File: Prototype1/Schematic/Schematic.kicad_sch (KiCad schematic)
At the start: 2 parts, among them P1 PMOD-Device-x2-Type-Generic-A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, U1 Teensy4.0

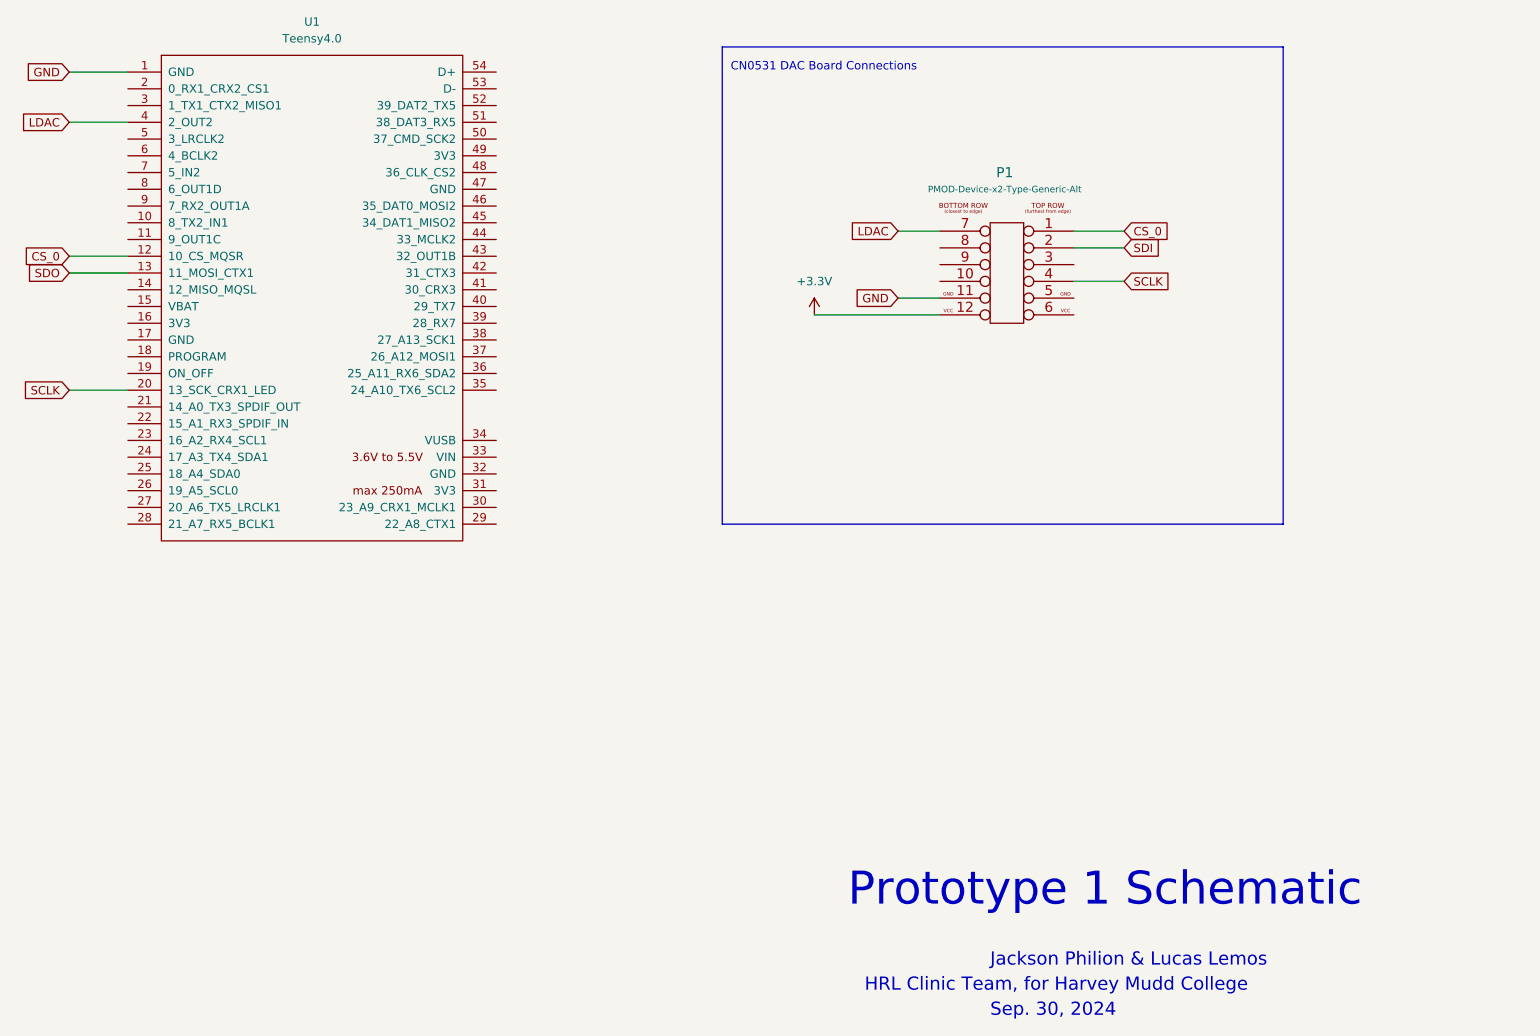
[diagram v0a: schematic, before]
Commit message: Add CD74 to Schematic
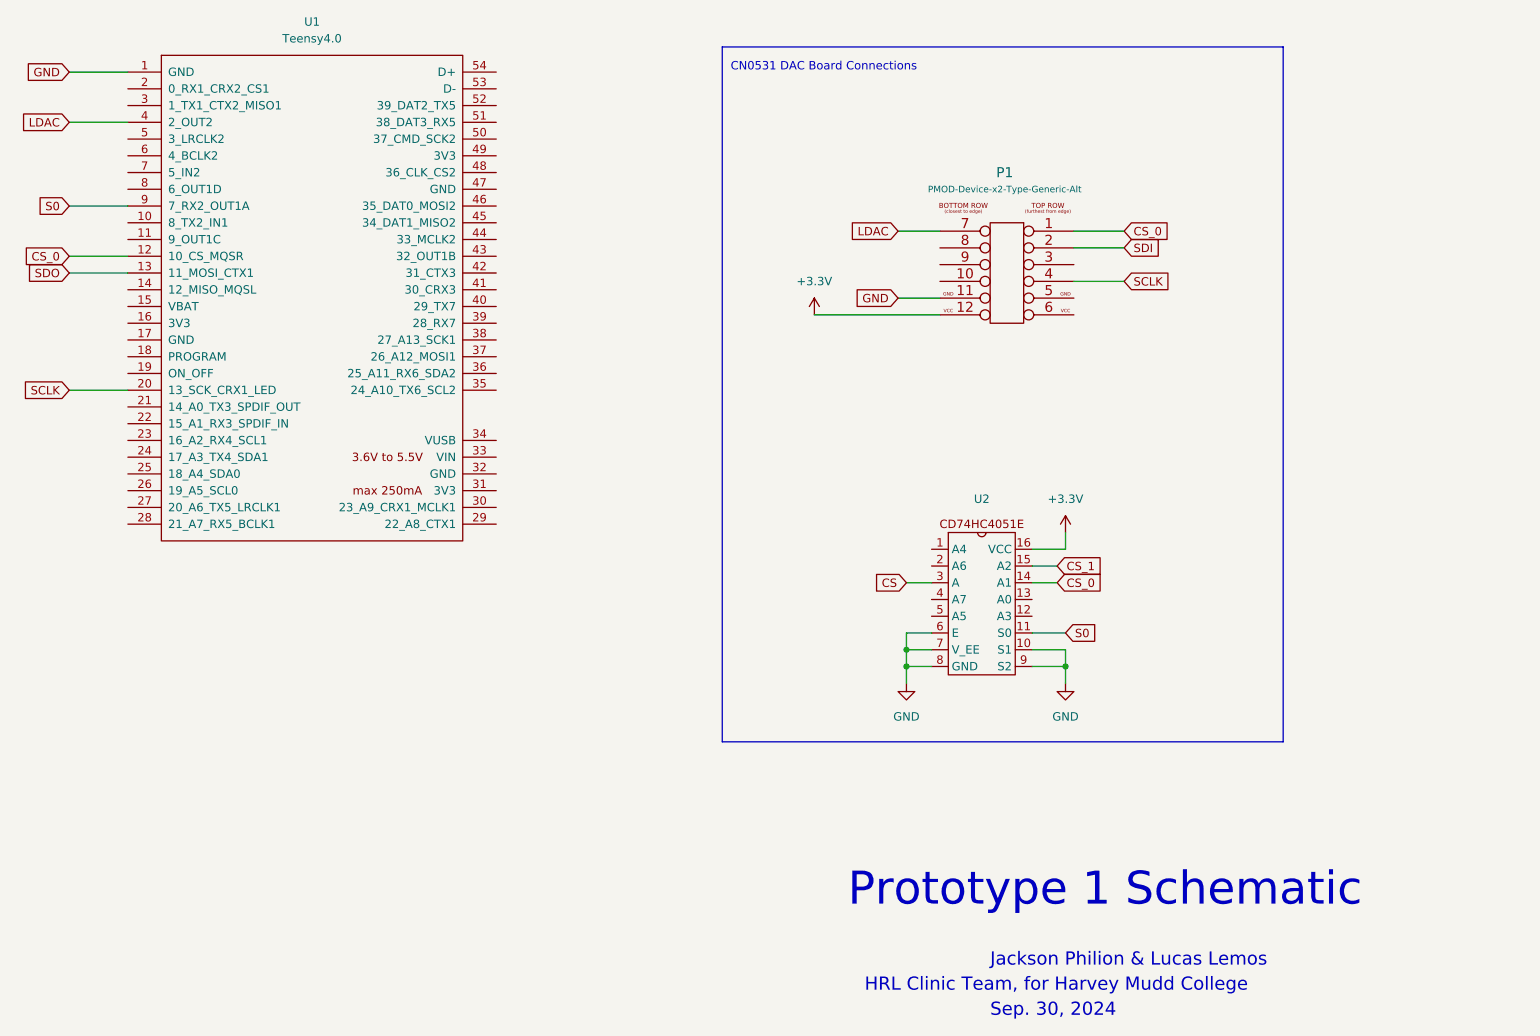
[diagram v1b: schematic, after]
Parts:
- added U2: ~, symbol HRL_Custom:CD74HC4051E
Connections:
- net +3.3V: now also U2.16 (VCC)
- net CS_0: now also U2.14 (A1)
- net GND: now also U2.10 (S1), U2.6 (E), U2.7 (V_EE), U2.8 (GND), U2.9 (S2)
- net S0: now reaches U1.9 (7_RX2_OUT1A)
- net S0: now also U2.11 (S0)
- new net CS: U2.3 (A)
- new net CS_1: U2.15 (A2)
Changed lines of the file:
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@@
 (kicad_sch (version 20230121) (generator eeschema)
   (paper "A4")
+  (junction (at 198.12 138.43) (diameter 0) (color 0 0 0 0)
+  )
+  (junction (at 198.12 140.97) (diameter 0) (color 0 0 0 0)
+  )
+  (junction (at 222.25 140.97) (diameter 0) (color 0 0 0 0)
+  )
+  (wire (pts (xy 198.12 138.43) (xy 198.12 140.97))
+    (stroke (width 0) (type default))
+  )
   (wire (pts (xy 71.12 58.42) (xy 80.01 58.42))
     (stroke (width 0) (type default))
   )
+  (wire (pts (xy 198.12 128.27) (xy 201.93 128.27))
+    (stroke (width 0) (type default))
+  )
+  (wire (pts (xy 222.25 140.97) (xy 222.25 143.51))
+    (stroke (width 0) (type default))
+  )
   (wire (pts (xy 223.52 74.93) (xy 231.14 74.93))
     (stroke (width 0) (type default))
@@
     (stroke (width 0) (type default))
   )
+  (wire (pts (xy 201.93 140.97) (xy 198.12 140.97))
+    (stroke (width 0) (type default))
+  )
   (wire (pts (xy 71.12 50.8) (xy 80.01 50.8))
     (stroke (width 0) (type default))
   )
+  (wire (pts (xy 222.25 138.43) (xy 222.25 140.97))
+    (stroke (width 0) (type default))
+  )
+  (wire (pts (xy 217.17 128.27) (xy 220.98 128.27))
+    (stroke (width 0) (type default))
+  )
   (wire (pts (xy 196.85 74.93) (xy 203.2 74.93))
     (stroke (width 0) (type default))
   )
+  (wire (pts (xy 201.93 138.43) (xy 198.12 138.43))
+    (stroke (width 0) (type default))
+  )
+  (wire (pts (xy 71.12 71.12) (xy 80.01 71.12))
+    (stroke (width 0) (type default))
+  )
+  (wire (pts (xy 217.17 135.89) (xy 222.25 135.89))
+    (stroke (width 0) (type default))
+  )
+  (wire (pts (xy 217.17 140.97) (xy 222.25 140.97))
+    (stroke (width 0) (type default))
+  )
   (wire (pts (xy 71.12 78.74) (xy 80.01 78.74))
     (stroke (width 0) (type default))
   )
+  (wire (pts (xy 198.12 135.89) (xy 198.12 138.43))
+    (stroke (width 0) (type default))
+  )
   (wire (pts (xy 71.12 81.28) (xy 80.01 81.28))
     (stroke (width 0) (type default))
   )
+  (wire (pts (xy 201.93 135.89) (xy 198.12 135.89))
+    (stroke (width 0) (type default))
+  )
+  (wire (pts (xy 217.17 138.43) (xy 222.25 138.43))
+    (stroke (width 0) (type default))
+  )
   (wire (pts (xy 223.52 77.47) (xy 231.14 77.47))
     (stroke (width 0) (type default))
@@
     (stroke (width 0) (type default))
   )
+  (wire (pts (xy 222.25 123.19) (xy 222.25 120.65))
+    (stroke (width 0) (type default))
+  )
   (wire (pts (xy 184.15 87.63) (xy 203.2 87.63))
     (stroke (width 0) (type default))
   )
-  (rectangle (start 170.18 46.99) (end 255.27 119.38)
+  (wire (pts (xy 217.17 123.19) (xy 222.25 123.19))
+    (stroke (width 0) (type default))
+  )
+  (wire (pts (xy 217.17 125.73) (xy 220.98 125.73))
+    (stroke (width 0) (type default))
+  )
+  (wire (pts (xy 198.12 140.97) (xy 198.12 143.51))
+    (stroke (width 0) (type default))
+  )
+  (rectangle (start 170.18 46.99) (end 255.27 152.4)
     (stroke (width 0) (type default))
     (fill (type none))
@@
     )
   )
+  (global_label "S0" (shape input) (at 71.12 71.12 180) (fields_autoplaced)
+    (effects (font (size 1.27 1.27)) (justify right))
+    (property "Intersheetrefs" "${INTERSHEET_REFS}" (at 65.7158 71.12 0)
+      (effects (font (size 1.27 1.27)) (justify right) hide)
+    )
+  )
   (global_label "SCLK" (shape input) (at 231.14 82.55 0) (fields_autoplaced)
     (effects (font (size 1.27 1.27)) (justify left))
@@
     )
   )
+  (global_label "CS_0" (shape input) (at 220.98 128.27 0) (fields_autoplaced)
+    (effects (font (size 1.27 1.27)) (justify left))
+    (property "Intersheetrefs" "${INTERSHEET_REFS}" (at 228.6218 128.27 0)
+      (effects (font (size 1.27 1.27)) (justify left) hide)
+    )
+  )
   (global_label "GND" (shape input) (at 71.12 50.8 180) (fields_autoplaced)
     (effects (font (size 1.27 1.27)) (justify right))
@@
     )
   )
+  (global_label "S0" (shape input) (at 222.25 135.89 0) (fields_autoplaced)
+    (effects (font (size 1.27 1.27)) (justify left))
+    (property "Intersheetrefs" "${INTERSHEET_REFS}" (at 227.6542 135.89 0)
+      (effects (font (size 1.27 1.27)) (justify left) hide)
+    )
+  )
+  (global_label "CS_1" (shape input) (at 220.98 125.73 0) (fields_autoplaced)
+    (effects (font (size 1.27 1.27)) (justify left))
+    (property "Intersheetrefs" "${INTERSHEET_REFS}" (at 228.6218 125.73 0)
+      (effects (font (size 1.27 1.27)) (justify left) hide)
+    )
+  )
   (global_label "LDAC" (shape input) (at 71.12 58.42 180) (fields_autoplaced)
     (effects (font (size 1.27 1.27)) (justify right))
@@
     (effects (font (size 1.27 1.27)) (justify right))
     (property "Intersheetrefs" "${INTERSHEET_REFS}" (at 64.3248 81.28 0)
+      (effects (font (size 1.27 1.27)) (justify right) hide)
+    )
+  )
+  (global_label "CS" (shape input) (at 198.12 128.27 180) (fields_autoplaced)
+    (effects (font (size 1.27 1.27)) (justify right))
+    (property "Intersheetrefs" "${INTERSHEET_REFS}" (at 192.6553 128.27 0)
       (effects (font (size 1.27 1.27)) (justify right) hide)
     )
@@
         (path "/4eb04ca2-2eee-448f-b097-610a5fc44453"
           (reference "P1") (unit 1)
+        )
+      )
+    )
+  )
+  (symbol (lib_id "power:GND") (at 222.25 143.51 0) (unit 1)
+    (in_bom yes) (on_board yes) (dnp no) (fields_autoplaced)
+    (property "Reference" "#PWR04" (at 222.25 149.86 0)
+      (effects (font (size 1.27 1.27)) hide)
+    )
+    (property "Value" "GND" (at 222.25 148.59 0)
+      (effects (font (size 1.27 1.27)))
+    )
+    (property "Footprint" "" (at 222.25 143.51 0)
+      (effects (font (size 1.27 1.27)) hide)
+    )
+    (property "Datasheet" "" (at 222.25 143.51 0)
+      (effects (font (size 1.27 1.27)) hide)
+    )
+    (pin "1")
+    (instances
+      (project "Schematic"
+        (path "/4eb04ca2-2eee-448f-b097-610a5fc44453"
+          (reference "#PWR04") (unit 1)
         )
       )
@@
         )
       )
+    )
+  )
+  (symbol (lib_id "power:+3.3V") (at 222.25 120.65 0) (unit 1)
+    (in_bom yes) (on_board yes) (dnp no) (fields_autoplaced)
+    (property "Reference" "#PWR03" (at 222.25 124.46 0)
+      (effects (font (size 1.27 1.27)) hide)
+    )
+    (property "Value" "+3.3V" (at 222.25 115.57 0)
+      (effects (font (size 1.27 1.27)))
+    )
+    (property "Footprint" "" (at 222.25 120.65 0)
+      (effects (font (size 1.27 1.27)) hide)
+    )
+    (property "Datasheet" "" (at 222.25 120.65 0)
+      (effects (font (size 1.27 1.27)) hide)
+    )
+    (pin "1")
+    (instances
+      (project "Schematic"
+        (path "/4eb04ca2-2eee-448f-b097-610a5fc44453"
+          (reference "#PWR03") (unit 1)
+        )
+      )
+    )
+  )
+  (symbol (lib_id "power:GND") (at 198.12 143.51 0) (unit 1)
+    (in_bom yes) (on_board yes) (dnp no) (fields_autoplaced)
+    (property "Reference" "#PWR02" (at 198.12 149.86 0)
+      (effects (font (size 1.27 1.27)) hide)
+    )
+    (property "Value" "GND" (at 198.12 148.59 0)
+      (effects (font (size 1.27 1.27)))
+    )
+    (property "Footprint" "" (at 198.12 143.51 0)
+      (effects (font (size 1.27 1.27)) hide)
+    )
+    (property "Datasheet" "" (at 198.12 143.51 0)
+      (effects (font (size 1.27 1.27)) hide)
+    )
+    (pin "1")
+    (instances
+      (project "Schematic"
+        (path "/4eb04ca2-2eee-448f-b097-610a5fc44453"
+          (reference "#PWR02") (unit 1)
+        )
+      )
+    )
+  )
+  (symbol (lib_name "CD74HC4051E_1") (lib_id "HRL_Custom:CD74HC4051E") (at 209.55 125.73 0) (unit 1)
+    (in_bom yes) (on_board yes) (dnp no) (fields_autoplaced)
+    (property "Reference" "U2" (at 209.55 115.57 0)
+      (effects (font (size 1.27 1.27)))
+    )
+    (property "Value" "~" (at 209.55 125.73 0)
+      (effects (font (size 1.27 1.27)))
+    )
+    (property "Footprint" "" (at 209.55 125.73 0)
+      (effects (font (size 1.27 1.27)) hide)
+    )
+    (property "Datasheet" "" (at 209.55 125.73 0)
+      (effects (font (size 1.27 1.27)) hide)
+    )
+    (pin "1")
+    (pin "10")
+    (pin "11")
+    (pin "12")
+    (pin "13")
+    (pin "14")
+    (pin "15")
+    (pin "16")
+    (pin "2")
+    (pin "3")
+    (pin "4")
+    (pin "5")
+    (pin "6")
+    (pin "7")
+    (pin "8")
+    (pin "9")
+    (instances
+      (project "Schematic"
+        (path "/4eb04ca2-2eee-448f-b097-610a5fc44453"
+          (reference "U2") (unit 1)
+        )
+      )
